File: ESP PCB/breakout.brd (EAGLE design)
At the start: 91.4 x 58.1 mm, 9 parts, among them X1 53047-04, X2 53047-04, X3 53047-04, X4 53047-04

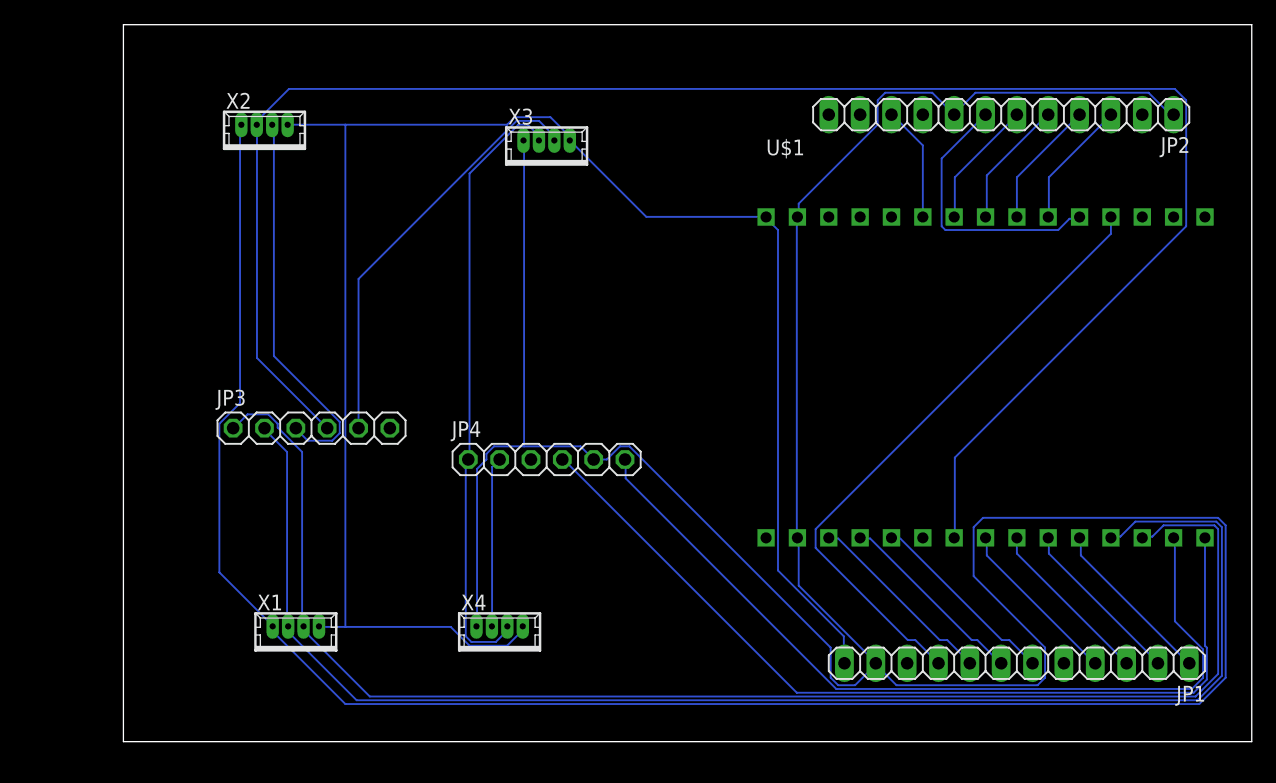
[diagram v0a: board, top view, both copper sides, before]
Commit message: update pcb remove cam
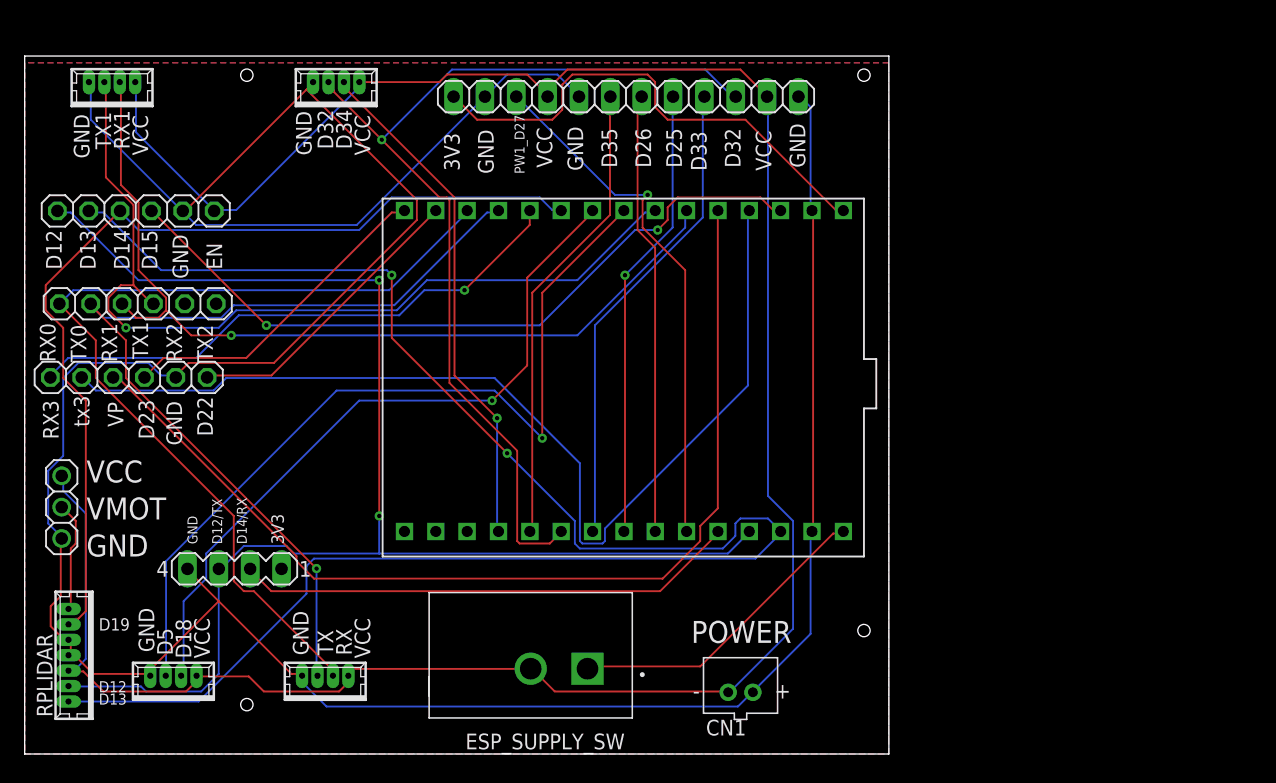
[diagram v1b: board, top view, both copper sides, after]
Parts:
- removed JP1: (no value), adafruit:1X12
- added CN1: (no value), adafruit:JST-PH-2-THM
- added ESP_SUPPLY_SW: GF-123-0054, GF-123-0054:SW_GF-123-0054
- added JP5: (no value), adafruit:1X06
- added MOTOR_VOLTAGE: (no value), adafruit:1X03
- added RPLIDAR: 53047-07, con-molex:53047-07
- added SV1: (no value), con-lstb:MA04-1
- moved JP4 34.5 mm to (0.43, 29.5)
- moved JP2 30.4 mm to (40.7, 52.3)
- moved U$1 27.2 mm to (58.3, 43.0), turned to 180 degrees
- moved X4 26.7 mm to (4.05, 4.89)
- moved X3 17.7 mm to (17.2, 53.0)
- moved JP3 17.3 mm to (1.16, 35.5)
- moved X2 12.8 mm to (-0.92, 53.0)
- moved X1 4.65 mm to (16.4, 4.89)
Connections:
- net PWM1 renamed D27
- removed net +5V: JP2.2
- removed net N$10: JP1.3, U$1.P$9
- removed net N$11: JP1.4, U$1.P$8
- removed net N$12: JP1.5
- removed net N$13: JP1.6, U$1.P$5
- removed net N$14: JP1.7, U$1.P$4
- removed net N$15: JP1.8, U$1.P$3
- removed net N$2: JP2.11
- removed net N$22: JP4.3
- removed net N$4: JP2.9
- removed net N$5: JP1.1, U$1.P$11
- removed net N$9: JP1.2, U$1.P$10
- removed net PWM: JP2.3, U$1.P$25
- removed net RX3: JP4.1, X3.3, X4.2
- removed net TEST: JP1.9, U$1.P$27
- removed net TX3: JP4.2, X4.3
- new net D12: JP5.1, RPLIDAR.6, SV1.3, U$1.P$19
- new net D13: JP5.2, RPLIDAR.7, U$1.P$18
- new net D14: SV1.2, U$1.P$20
- new net D15: JP5.4, U$1.P$3
- new net D18: U$1.P$9, X4.2
- new net D19: JP5.3, RPLIDAR.2, U$1.P$10
- new net D2: JP4.2, U$1.P$4
- new net D21: JP4.1, U$1.P$11
- new net D32: JP2.3, U$1.P$25, X3.3
- new net D34: U$1.P$27, X3.2
- new net D4: JP4.3, U$1.P$5
- new net D5: U$1.P$8, X4.3
- new net EN: U$1.P$30
- new net VESP: ESP_SUPPLY_SW.1, U$1.P$16
- new net VMOT: MOTOR_VOLTAGE.2, RPLIDAR.1
- new net VN: U$1.P$28
- new net VP: U$1.P$29
- net 3V3: now also SV1.1; no longer JP1.10
- net GND: now also CN1.1, JP2.11, JP5.5, MOTOR_VOLTAGE.1, RPLIDAR.3, RPLIDAR.4, SV1.4; no longer JP1.11
- net N$1: now also U$1.P$1
- net RX2: no longer X3.2
- net VCC: now also CN1.2, ESP_SUPPLY_SW.2, JP2.2, JP2.9, JP5.6, MOTOR_VOLTAGE.3, RPLIDAR.5; no longer JP1.12, U$1.P$16
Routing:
- net D13: track 0.00 -> 138.3 mm, vias 0 -> 2
- net D12: track 0.00 -> 116.8 mm, vias 0 -> 2
- net GND: track 346.2 -> 259.7 mm
- net D2: track 0.00 -> 84.2 mm
- net D4: track 0.00 -> 83.2 mm
- net D32: track 0.00 -> 80.0 mm, vias 0 -> 1
- net D19: track 0.00 -> 76.0 mm
- net TX1: track 147.2 -> 72.0 mm, vias 0 -> 1
- net D5: track 0.00 -> 68.3 mm, vias 0 -> 1
- net D15: track 0.00 -> 60.2 mm, vias 0 -> 2
- net D18: track 0.00 -> 57.8 mm, vias 0 -> 1
- net VCC: track 140.0 -> 192.2 mm
- net TEST: track 50.6 -> 0.00 mm
- net RX3: track 50.0 -> 0.00 mm
- net D23: track 72.0 -> 26.8 mm
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- added copper zone on layer 16, net GND
- added copper zone on layer 1, net VCC
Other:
- board size 91.4 x 58.1 mm -> 70 x 56.5 mm
- board text added: "3V3"
- board text added: "D12"
- board text added: "D12/TX"
- board text added: "D13"
- board text added: "D14"
- board text added: "D14/RX"
- board text added: "D15"
- board text added: "D18"
- board text added: "D19"
- board text added: "D22"
- board text added: "D23"
- board text added: "D25"
- board text added: "D26"
- board text added: "D32"
- board text added: "D33"
- board text added: "D34"
- board text added: "D35"
- board text added: "D5"
- board text added: "EN"
- board text added: "GND"
- board text added: "POWER"
- board text added: "PW1_D27"
- board text added: "RX"
- board text added: "RX0"
- board text added: "RX1"
- board text added: "RX2"
- board text added: "RX3"
- board text added: "TX"
- board text added: "TX0"
- board text added: "TX1"
- board text added: "TX2"
- board text added: "VCC"
- board text added: "VMOT"
- board text added: "VP"
- board text added: "tx3"
